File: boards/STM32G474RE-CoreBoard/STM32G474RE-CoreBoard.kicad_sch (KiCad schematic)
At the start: 33 parts, among them J1 USB-C, J2 PORT_L, J3 PORT_B, J4 PORT_R, J5 PORT_T, J6 DEBUG, SW1 RESET, SW2 BOOT0, U1 STM32G474RET6, U2 AP2112K-3.3, Y1 8MHz, Y2 32.768kHz

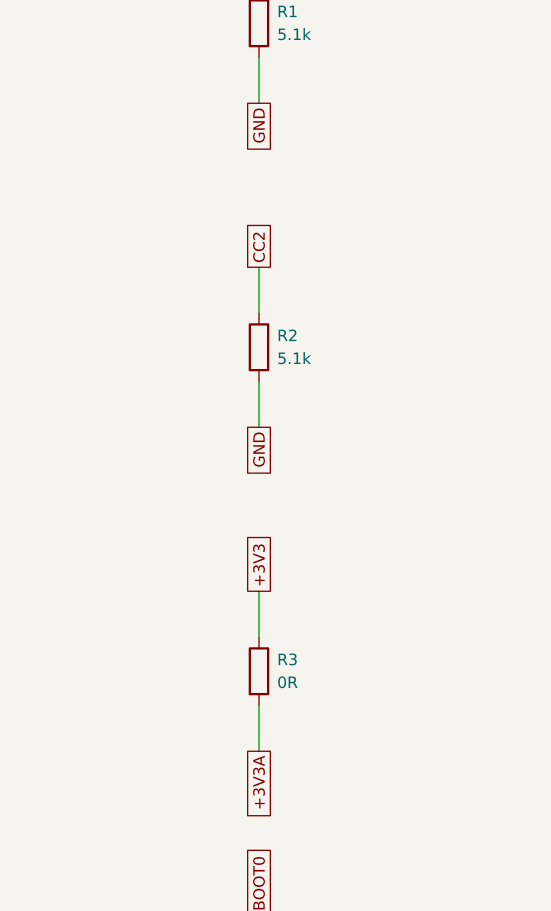
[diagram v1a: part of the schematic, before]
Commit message: Довести G474 до чистого DRC KiCad при штатных 0.2 мм
Раньше плата разводилась под 0.15 мм и правило проекта подгонялось под
геометрию. Теперь наоборот - геометрия приведена к стандартным 0.2 мм,
правило вернулось к значению по умолчанию.

- сигнальные дорожки 0.2 -> 0.15 мм: при шаге выводов LQFP64 0.5 мм
  ширина 0.2 не оставляла 0.2 мм зазора в расходящемся веере
- USB D+/D- 0.18 -> 0.14 мм: via D+ проходила в 0.185 мм от дорожки D-
- via земли внутри корпуса смещены перпендикулярно от вывода питания
  своей пары, отвод идёт сперва прямо внутрь и лишь потом наискось
- верхняя via VBUS отодвинута от земляного пада USB-C

Заодно закрыты замечания сверки платы со схемой:
- футпринтам проставлено имя библиотеки в FPID
- значения D1 и R3 приведены к схемным (LED, 0R/FB); на шелке у R3
  по-прежнему короткое 0R
- монтажные отверстия H1-H4 добавлены в схему

Проверка: зазоры 0 нарушений при 0.2 мм, несоединённых 0, courtyard 0,
шелкография 0, hole-to-hole минимум 0.716 мм.

Co-Authored-By: Claude Opus 5 <noreply@anthropic.com>
Claude-Session: https://claude.ai/code/session_014TdfexXmnKj4uq4WkX48Er
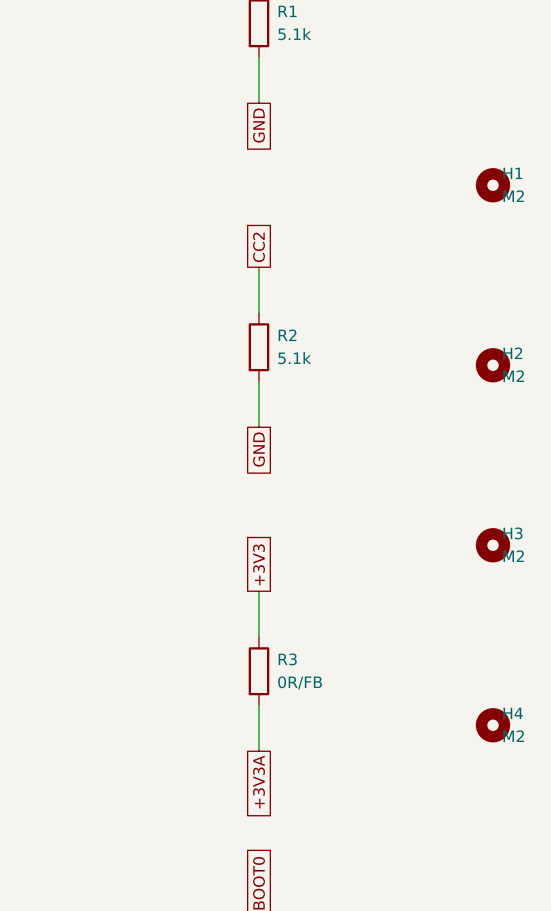
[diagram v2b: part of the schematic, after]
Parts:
- added H1, H2, H3, H4: M2, MountingHole:MountingHole_2.2mm_M2, symbol Mechanical:MountingHole
- C1, C13, C14, C15, C16, C17, C2, C3, C4, C9: footprint :C_0402_1005Metric -> Capacitor_SMD:C_0402_1005Metric
- C10, C6: footprint :C_0603_1608Metric -> Capacitor_SMD:C_0603_1608Metric
- C5, C7, C8: footprint :C_0805_2012Metric -> Capacitor_SMD:C_0805_2012Metric
- R3: value 0R -> 0R/FB

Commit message: Перевести проект на собственную библиотеку футпринтов
KiCad сверяет футпринты платы с библиотечными, а системные библиотеки
меняются от версии к версии: KiCad 10 у пользователя давал 31
предупреждение lib_footprint_mismatch против копий из KiCad 7.

Генератор теперь выгружает все 14 использованных футпринтов в
auto_probe.pretty рядом с платой и прописывает fp-lib-table. Плата и
схема ссылаются на эту библиотеку. Копии снимаются уже после всех
доработок, поэтому в них попадает и сплошное соединение земли USB-C,
и снятая с края шелкография, и подменённая 3D-модель.

Побочный эффект - проект перестал зависеть от системных библиотек
KiCad вообще: собирается одинаково у любого, кто его клонирует.

Co-Authored-By: Claude Opus 5 <noreply@anthropic.com>
Claude-Session: https://claude.ai/code/session_014TdfexXmnKj4uq4WkX48Er
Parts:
- C1, C13, C14, C15, C16, C17, C2, C3, C4, C9: footprint Capacitor_SMD:C_0402_1005Metric -> auto_probe:C_0402_1005Metric
- C10, C6: footprint Capacitor_SMD:C_0603_1608Metric -> auto_probe:C_0603_1608Metric
- C5, C7, C8: footprint Capacitor_SMD:C_0805_2012Metric -> auto_probe:C_0805_2012Metric
- D1: footprint LED_SMD:LED_0805_2012Metric -> auto_probe:LED_0805_2012Metric
- H1, H2, H3, H4: footprint MountingHole:MountingHole_2.2mm_M2 -> auto_probe:MountingHole_2.2mm_M2
- J1: footprint Connector_USB:USB_C_Receptacle_HRO_TYPE-C-31-M-12 -> auto_probe:USB_C_Receptacle_HRO_TYPE-C-31-M-12
- J2, J3, J4, J5: footprint Connector_PinHeader_2.54mm:PinHeader_1x16_P2.54mm_Vertical -> auto_probe:PinHeader_1x16_P2.54mm_Vertical
- J6: footprint Connector_PinHeader_2.54mm:PinHeader_1x10_P2.54mm_Vertical -> auto_probe:PinHeader_1x10_P2.54mm_Vertical
- R1, R2, R3, R4, R5: footprint Resistor_SMD:R_0402_1005Metric -> auto_probe:R_0402_1005Metric
- SW1, SW2: footprint Button_Switch_SMD:SW_SPST_SKQG_WithoutStem -> auto_probe:SW_SPST_SKQG_WithoutStem
- U1: footprint Package_QFP:LQFP-64_10x10mm_P0.5mm -> auto_probe:LQFP-64_10x10mm_P0.5mm
- U2: footprint Package_TO_SOT_SMD:SOT-23-5 -> auto_probe:SOT-23-5
- Y1: footprint Crystal:Crystal_SMD_5032-2Pin_5.0x3.2mm -> auto_probe:Crystal_SMD_5032-2Pin_5.0x3.2mm
- Y2: footprint Crystal:Crystal_SMD_MicroCrystal_CC7V-T1A-2Pin_3.2x1.5mm -> auto_probe:Crystal_SMD_MicroCrystal_CC7V-T1A-2Pin_3.2x1.5mm

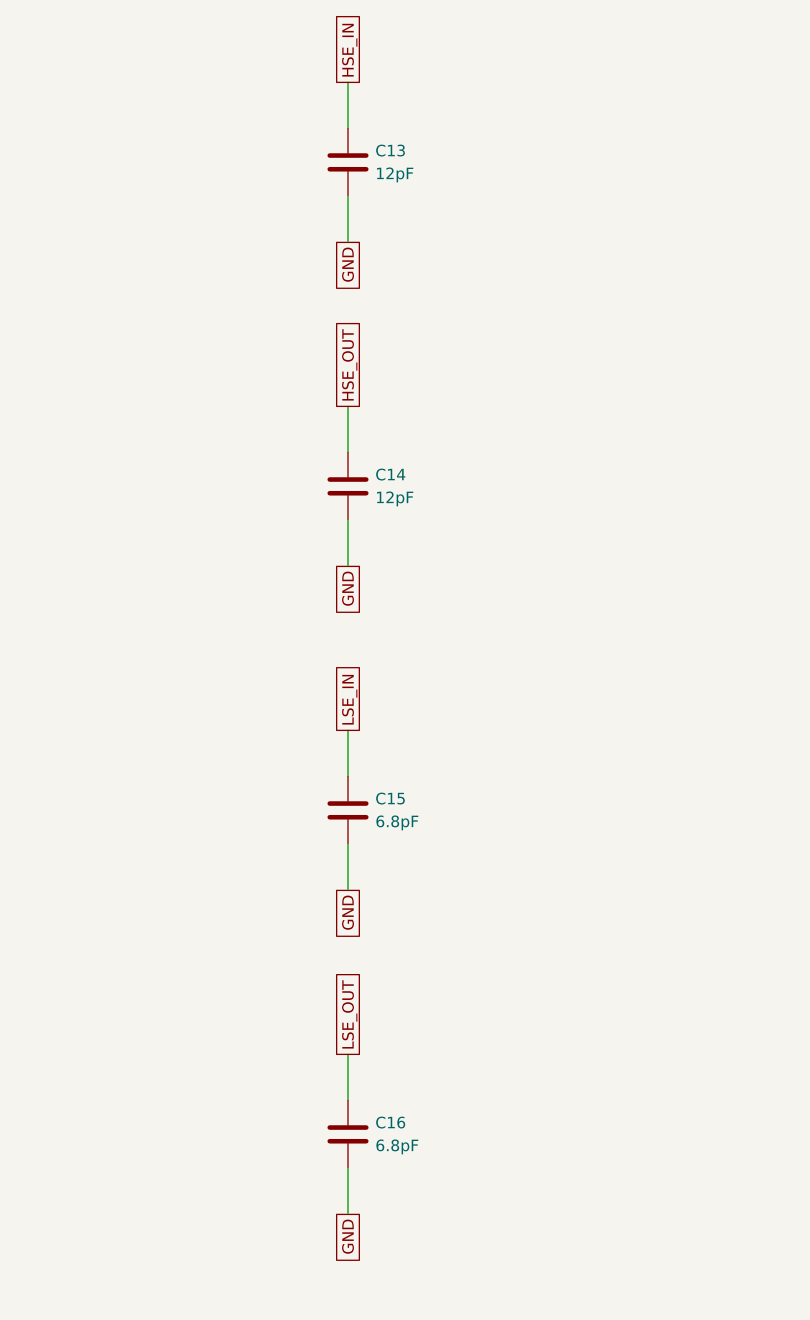
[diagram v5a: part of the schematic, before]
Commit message: G474: подготовка к заказу JLCPCB - кварцы под склад, легенда на шелкографии
Кварцы подобраны по наличию: HSE 8 МГц X50328MSB2GI (C115962, Basic, CL 20 пФ)
с обвязкой 33 пФ (C1562, Basic) вместо 12 пФ; LSE остался C97606 (CL 12.5 пФ),
обвязка 6.8 пФ -> 18 пФ как на H723. Номиналы исправлены в схеме, плате и на
шелкографии, цепи не менялись.

Шелкография: номиналы у деталей заменены легендой на нижней стороне (стиль
H723, компактнее), у компонентов остались только обозначения; четыре рефа
раздвинуты от падов.

Генератор:
- ROT_FIX в export.py теперь по имени корпуса, а не по рефу (LQFP -90,
  SOT-23-8 +180 - проверено заказами H723 и CAN-Unit);
- примечания о нагрузочной ёмкости кварцев - по номиналу (CL_NOTE),
  новые номера LCSC: 33 пФ, 120R, TCAN332G, MSK12C02;
- паяные перемычки (SolderJumper) исключаются из BOM.

H723: выходные файлы перегенерированы, содержимое эквивалентно.

Co-Authored-By: Claude Fable 5 <noreply@anthropic.com>
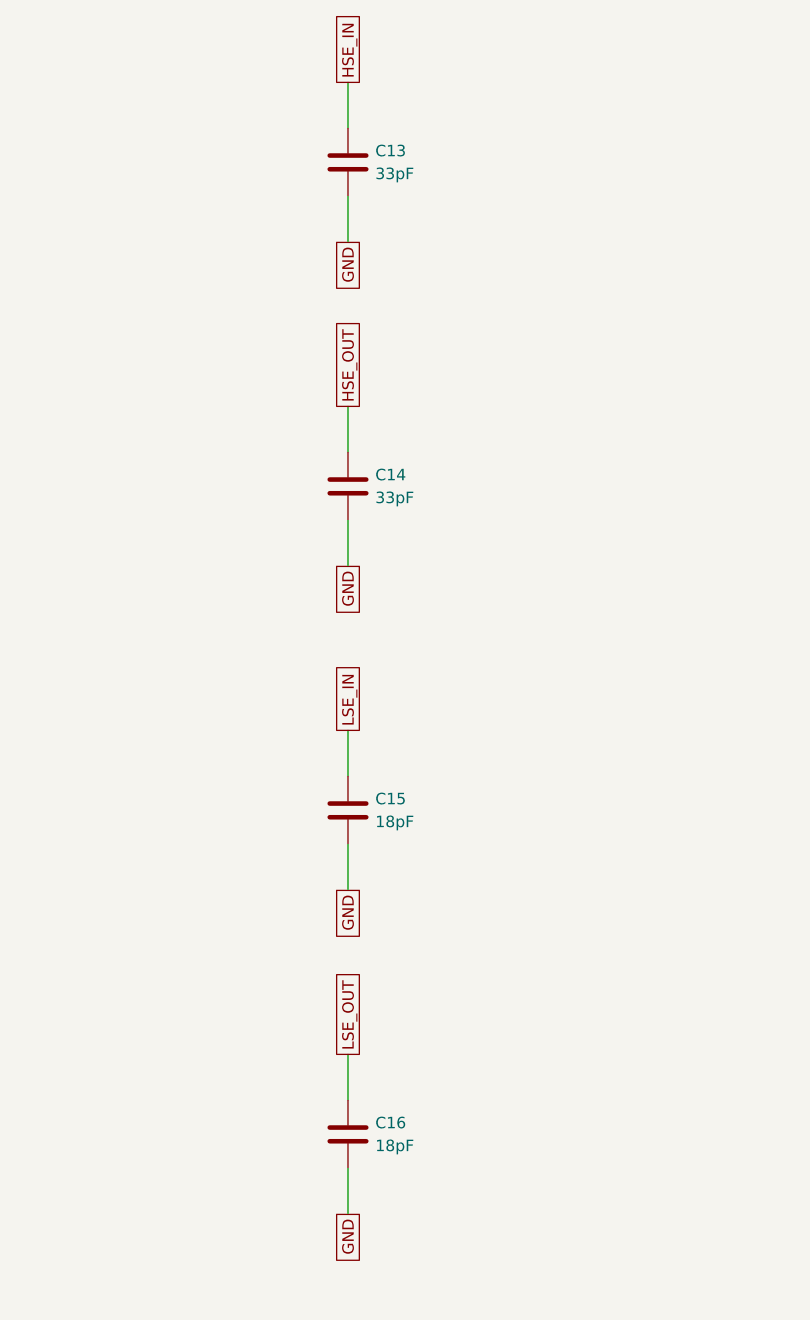
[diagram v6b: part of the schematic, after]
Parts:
- C13, C14: value 12pF -> 33pF
- C15, C16: value 6.8pF -> 18pF
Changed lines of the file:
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@@
       (effects (font (size 1.27 1.27)) (justify left))
     )
-    (property "Value" "12pF" (at 467.032 145.27 0)
+    (property "Value" "33pF" (at 467.032 145.27 0)
       (effects (font (size 1.27 1.27)) (justify left))
     )
@@
       (effects (font (size 1.27 1.27)) (justify left))
     )
-    (property "Value" "12pF" (at 467.032 181.27 0)
+    (property "Value" "33pF" (at 467.032 181.27 0)
       (effects (font (size 1.27 1.27)) (justify left))
     )
@@
       (effects (font (size 1.27 1.27)) (justify left))
     )
-    (property "Value" "6.8pF" (at 467.032 217.27 0)
+    (property "Value" "18pF" (at 467.032 217.27 0)
       (effects (font (size 1.27 1.27)) (justify left))
     )
@@
       (effects (font (size 1.27 1.27)) (justify left))
     )
-    (property "Value" "6.8pF" (at 467.032 253.27 0)
+    (property "Value" "18pF" (at 467.032 253.27 0)
       (effects (font (size 1.27 1.27)) (justify left))
     )
